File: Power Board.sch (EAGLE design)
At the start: 36 parts, among them Q1 IRLB8743PBF, U1 S18V20F12, U2 D24V22F3, U3 D24V22F5, U4 LTC7004, U5 CD4011BPWR

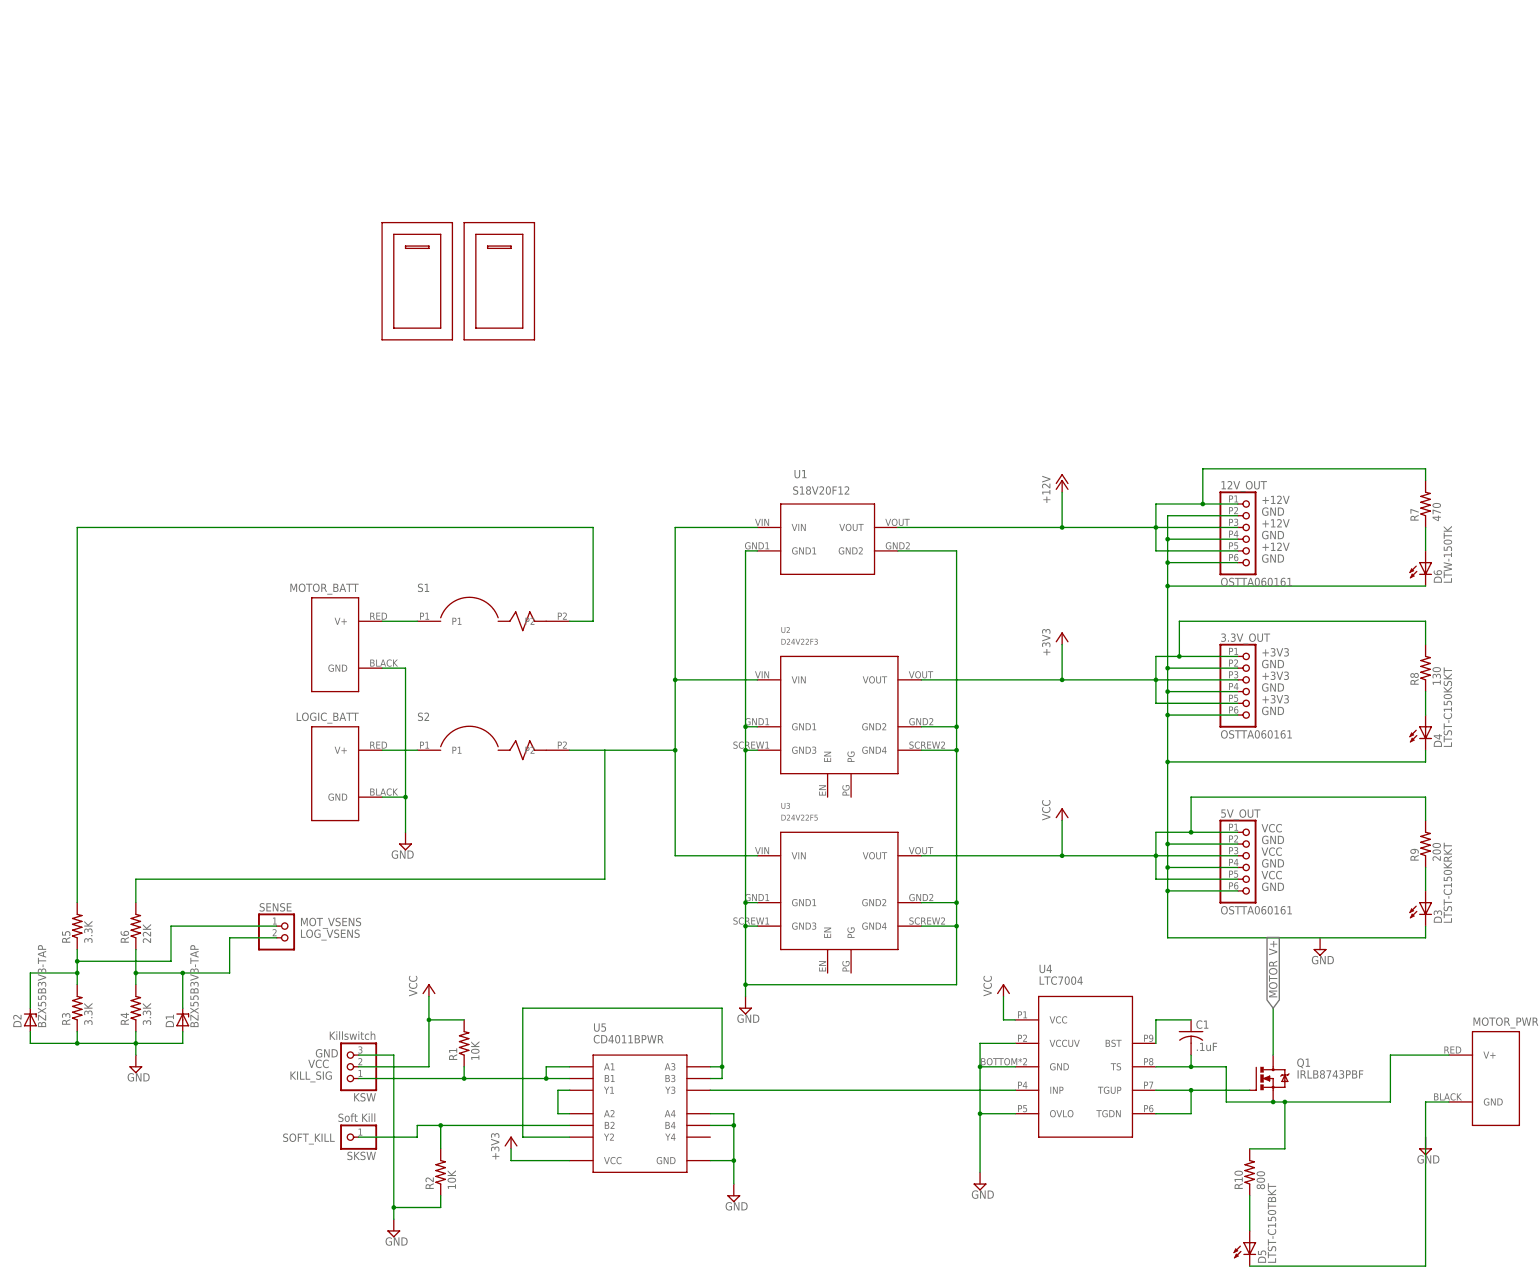
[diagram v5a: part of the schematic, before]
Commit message: Add Simple Switcher 5V regulator design (still needs to be CADed)
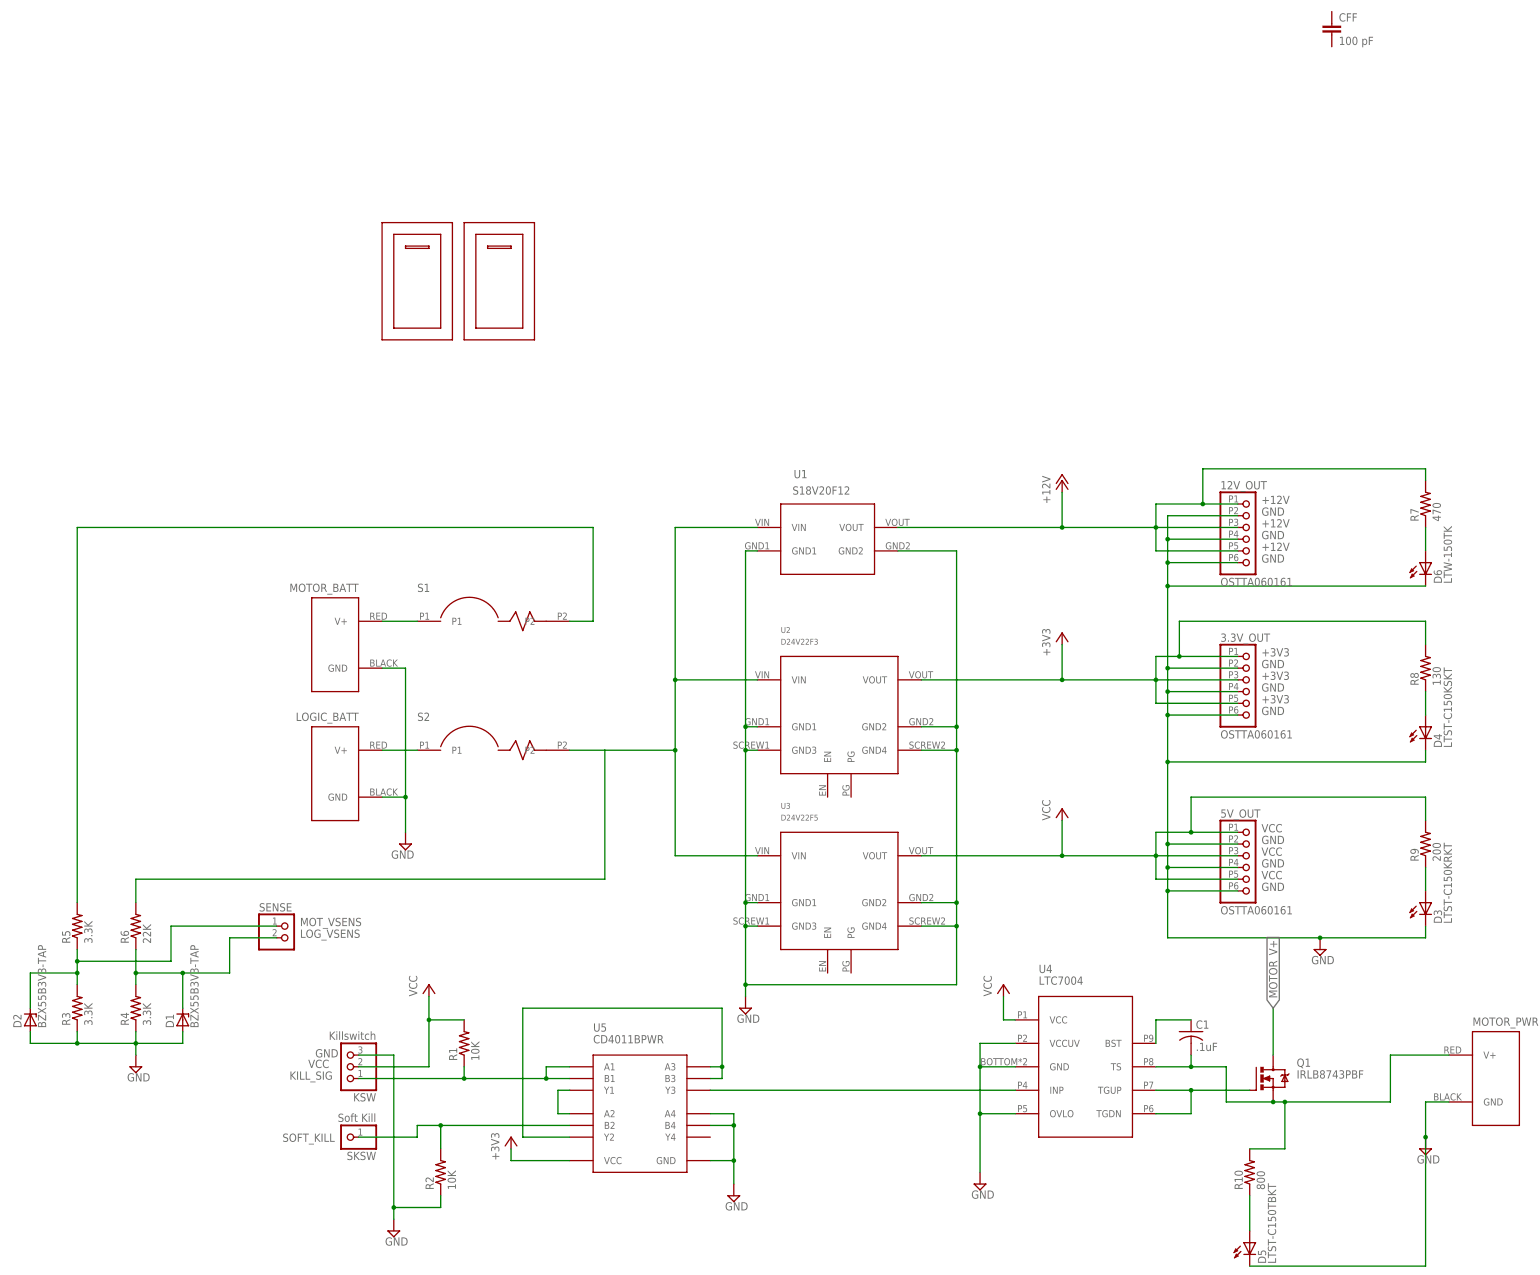
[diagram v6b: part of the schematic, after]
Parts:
- added CFF: 100 pF, rcl:C-EUC1206

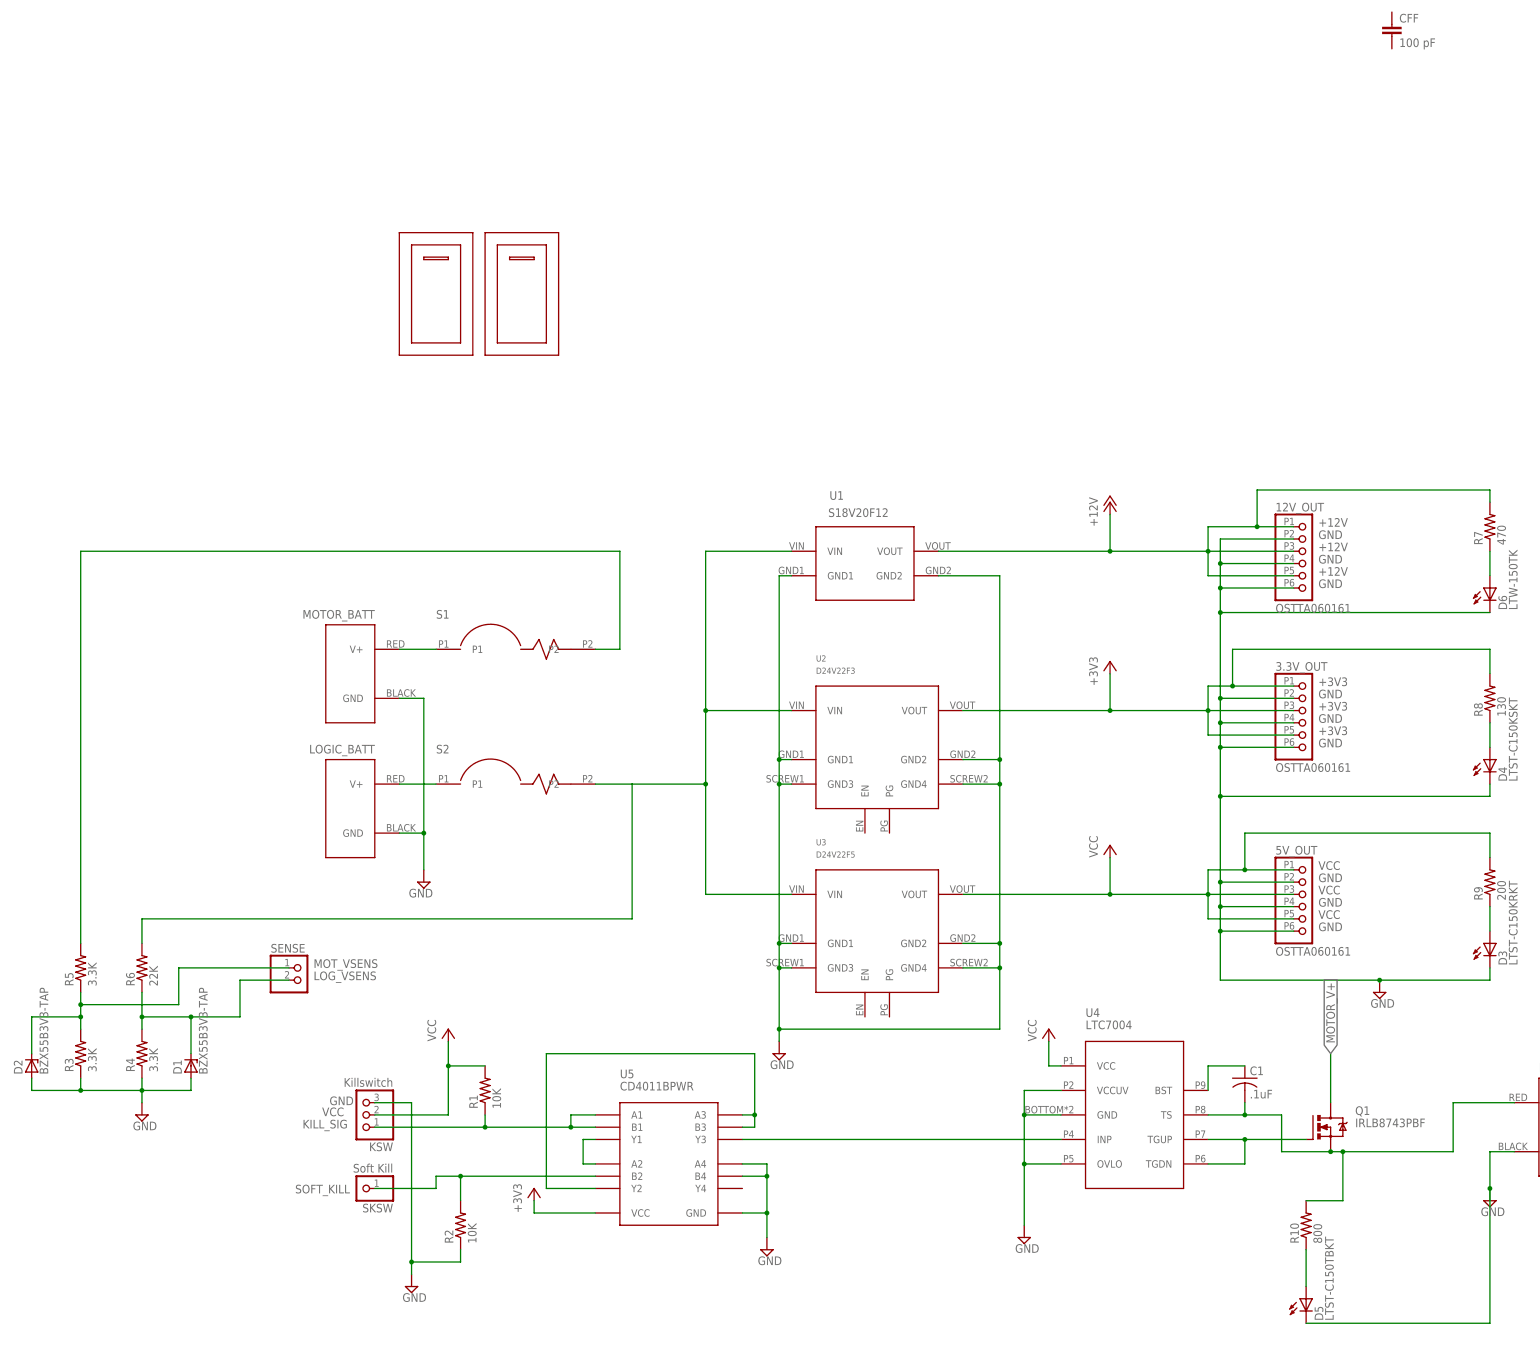
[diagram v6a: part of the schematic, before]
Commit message: Reroute top of board for new surface-mount parts
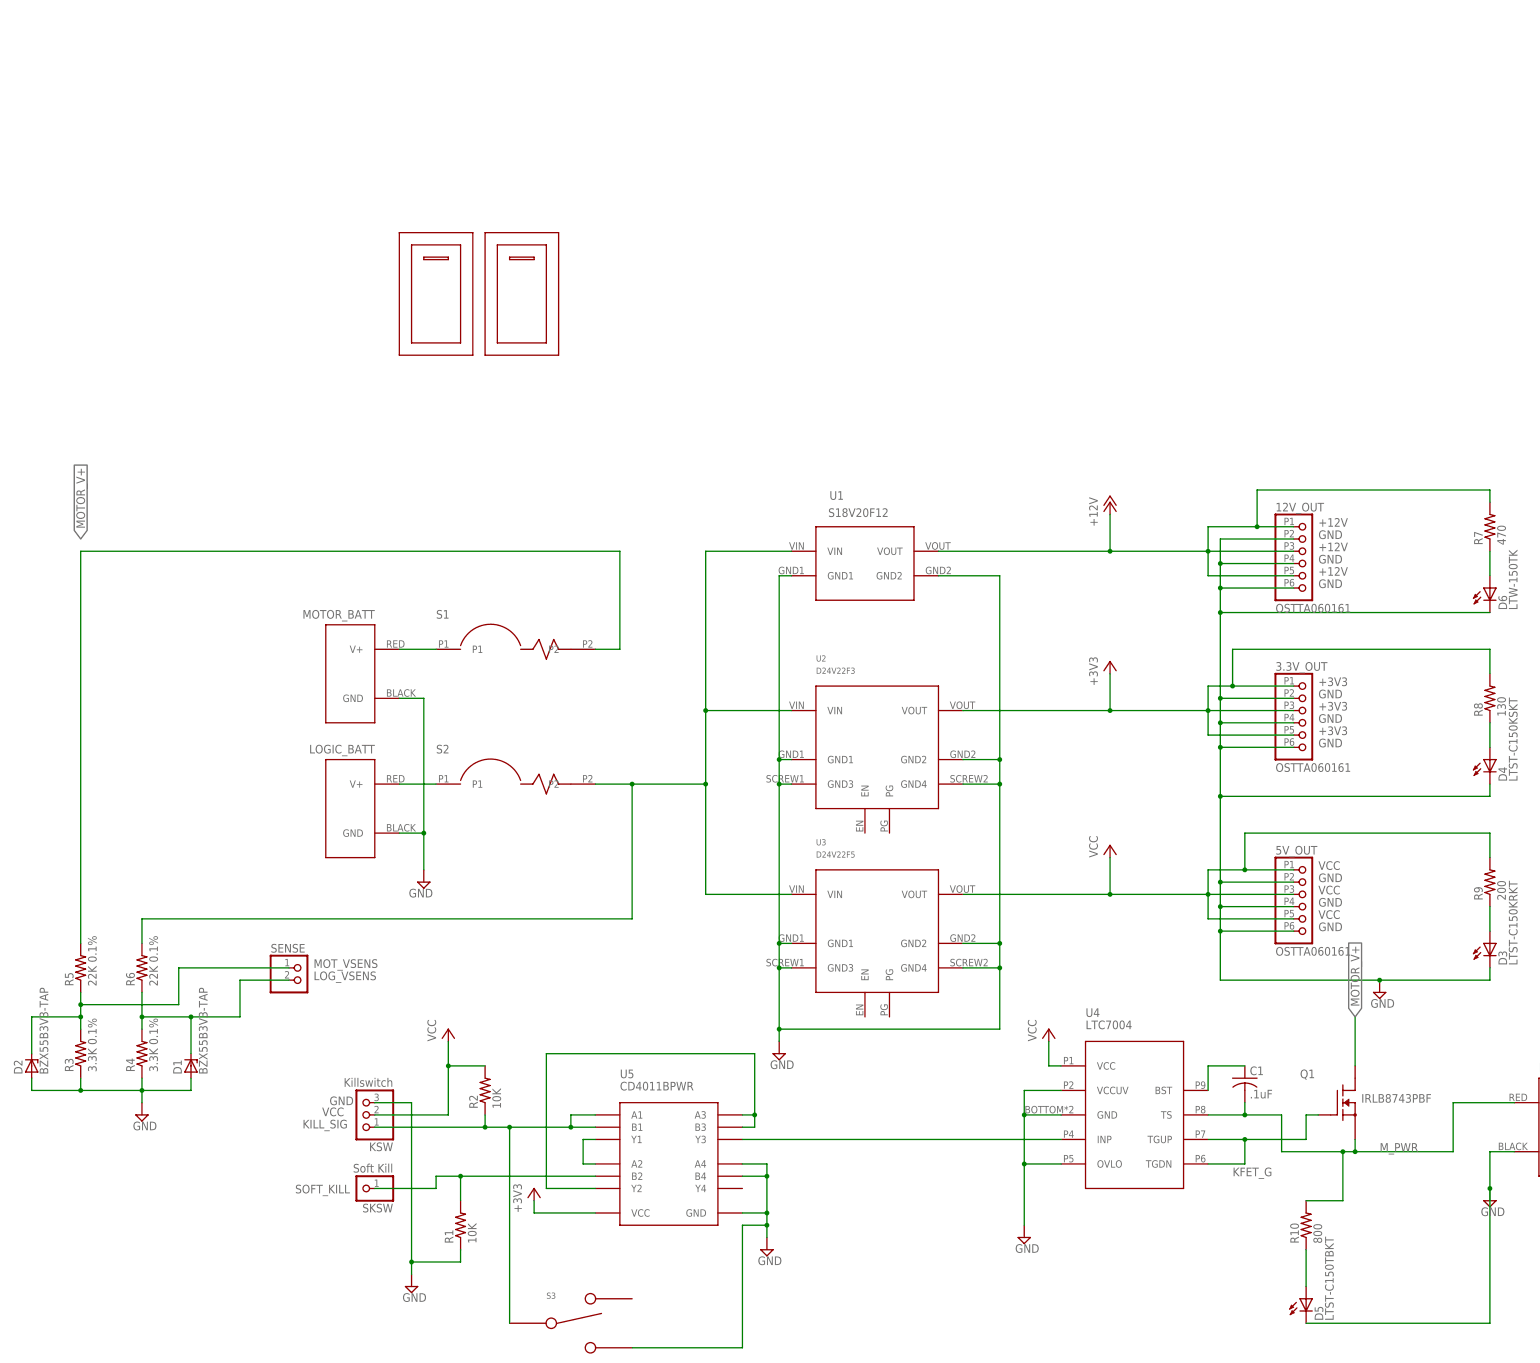
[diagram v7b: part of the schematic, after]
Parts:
- removed CFF: 100 pF, rcl:C-EUC1206
- added S3: OS102011MS2QN1, Power Board Custom:OS102011MS2QN1
- Q1: device transistor-power:IRF520 -> Power Board Custom:IRLB8743PBF
- R1, R2: device resistor:R-US_0207/10 -> rcl:R-US_R1206
- R3, R4: value 3.3K -> 3.3K 0.1%
- R5: value 3.3K -> 22K 0.1%
- R6: value 22K -> 22K 0.1%
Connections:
- net N$8 renamed KFET_G
- net N$9 renamed M_PWR
- net GND: now also R1.1, S3.L; no longer R2.1
- net KILL_SIG: now also R2.1, S3.C; no longer R1.1
- net SOFT_KILL: now also R1.2; no longer R2.2
- net VCC: now also R2.2; no longer R1.2
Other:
- moved on the sheet: R1, R2
